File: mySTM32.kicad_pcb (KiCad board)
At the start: 2 copper layers, 138 x 108 mm, 122 parts, among them J1 conn1X2, J10 DB9_Female****, J11 USB_OTG, J12 conn2X16, J13 conn2X3, J14 Conn_02x02, J15 conn2X3, J16 conn1X2, J17 conn2X2, J18 JTAG, J19 Conn_02x17_Odd_Even, J2 USB_OTG, J20 Conn_02x22_Odd_Even, J21 conn2X9, J22 conn2X3, J23 Conn2x4, J3 conn2X3, J4 conn2X2, J5 conn2X2, J6 conn1X2, J7 Conn_01x02, J8 Conn2x4, J9 conn2X4, Q1 Q_NPN_BEC(S8050), Q2 Q_NPN_BEC, Q3 Q_NPN_BEC(S8050), SW1 KFT8.0, SW2 WAKUP, SW3 RESET, SW4 KE1, SW5 KEY2, U1 AT24C02, U2 W25Q16, U3 SD-Card, U4 SP3485, U5 SN65HVD230, U6 CH340G, U7 AMS1117, U8 SP3232, U9 STM32F103VET6, Y1 12MHz, Y2 32.768KHz, Y3 8MHz

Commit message: [sd-card]
Signed-off-by: EasonLiang <liangyx25@163.com>
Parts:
- moved R11 1.55 mm to (86.7, 61.9)
- moved R13 1.52 mm to (101.4, 61.8)
- moved R10 1.47 mm to (84.2, 61.9)
- moved R14 1.46 mm to (81.7, 61.9)
- moved R12 1.19 mm to (99.2, 61.9)
- moved C8 0.86 mm to (92.5, 61.1), turned to 0 degrees
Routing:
- net /PC8: track 26.4 -> 89.6 mm, vias 0 -> 1
- net /PC10: track 25.5 -> 84.2 mm, vias 0 -> 2
- net /PC9: track 23.3 -> 79.8 mm, vias 0 -> 1
- net /PC11: track 22.6 -> 76.4 mm, vias 0 -> 2
- net /PC12: track 26.4 -> 78.5 mm, vias 0 -> 1
- net /PD2: track 25.6 -> 75.7 mm, vias 0 -> 2
- net +3V3: track 262.6 -> 287.4 mm
- net /KEY1: track 34.5 -> 39.8 mm
- net /JTDI: track 76.9 -> 81.5 mm
- net /JTCK_SWCLK: track 77.0 -> 79.6 mm
- net /JTMS_SWDIO: track 74.9 -> 77.2 mm
- net /OV_PE6: track 51.8 -> 50.0 mm
- net /JTDO: track 84.3 -> 84.9 mm

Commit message: [Camera]
Signed-off-by: EasonLiang <liangyx25@163.com>
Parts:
- moved J23 6.20 mm to (54.1, 36.4)
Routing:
- net /OV_PC7: track 23.4 -> 115.3 mm, vias 0 -> 2
- net /OV_PC6: track 26.5 -> 112.7 mm, vias 0 -> 2
- net /NRF_CSN: track 50.1 -> 123.9 mm
- net /NRF_CE: track 0.00 -> 69.9 mm
- net /NRF_IRQ: track 0.00 -> 66.7 mm
- net /OV_PC5: track 30.2 -> 96.2 mm, vias 0 -> 1
- net /OV_PC4: track 32.5 -> 95.9 mm
- net /OV_PC3: track 30.2 -> 89.9 mm, vias 0 -> 1
- net /OV_PC1: track 30.5 -> 82.8 mm, vias 0 -> 2
- net /OV_PE6: track 50.0 -> 101.1 mm
- net /OV_PE4: track 50.0 -> 100.1 mm
- net /OV_PE3: track 47.0 -> 96.9 mm
- net /OV_PE5: track 46.9 -> 96.9 mm
- net /OV_PC2: track 33.3 -> 81.7 mm, vias 0 -> 1
- net /OV_PC0: track 34.1 -> 82.2 mm, vias 0 -> 2
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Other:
- board text added: "PC0"
- board text added: "PC1"
- board text added: "PC2"
- board text added: "PC3"
- board text added: "PC4"
- board text added: "PC5"
- board text added: "PC6"
- board text added: "PC7"
- board text added: "PE0"
- board text added: "PE1"
- board text added: "PE2"
- board text added: "PE3"
- board text added: "PE4"
- board text added: "PE5"
- board text added: "PE6"
- board text added: "X"

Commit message: [RF2.4G]
Signed-off-by: EasonLiang <liangyx25@163.com>
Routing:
- net /PA6: track 52.0 -> 137.4 mm, vias 0 -> 1
- net /PA7: track 51.6 -> 136.7 mm, vias 0 -> 1
- net /PA5: track 52.3 -> 132.8 mm, vias 0 -> 1
- net +3V3: track 287.3 -> 363.9 mm
- net GND: track 121.3 -> 123.0 mm, vias 2 -> 3
- net /FLASH_CS: track 16.6 -> 18.1 mm
- net /FLASH_MOSI: track 10.3 -> 11.7 mm
- net /OV_PC3: track 89.9 -> 91.0 mm, vias 1 -> 2
- net /FLASH_CLK: track 9.83 -> 10.4 mm, vias 0 -> 1
- net /KEY1: vias 1 -> 2

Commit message: [TFT-LCD]
Signed-off-by: EasonLiang <liangyx25@163.com>
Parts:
- moved SW2 15.0 mm to (82.9, 132.7)
- moved SW3 14.9 mm to (68.0, 132.7)
- moved R21 4.91 mm to (117.3, 121.2), turned to 0 degrees
- moved C22 1.15 mm to (102.5, 109.7), turned to 180 degrees
- moved R19 0.20 mm to (75.3, 125.6)
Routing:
- net /FSMC_NE1: track 32.3 -> 84.7 mm, vias 0 -> 2
- net /FSMC_NOE: track 27.0 -> 73.8 mm, vias 0 -> 2
- net /DB2: track 24.1 -> 70.6 mm, vias 0 -> 2
- net /FSMC_NWE: track 30.8 -> 75.5 mm, vias 0 -> 2
- net /DB3: track 27.9 -> 72.3 mm, vias 0 -> 2
- net /FSMC_A16: track 26.5 -> 70.3 mm, vias 0 -> 2
- net /BL_CTR: track 26.2 -> 67.7 mm, vias 0 -> 1
- net /DB4: track 33.1 -> 70.4 mm, vias 0 -> 1
- net /DB6: track 34.6 -> 71.1 mm, vias 0 -> 1
- net /DB5: track 36.9 -> 72.5 mm, vias 0 -> 1
- net /RESET: track 14.7 -> 49.1 mm, vias 0 -> 1
- net /DB8: track 38.1 -> 72.5 mm, vias 0 -> 1
- net +3V3: track 363.9 -> 397.0 mm
- net /DB0: track 27.3 -> 59.4 mm, vias 0 -> 2
- net /DB10: track 37.5 -> 68.6 mm, vias 0 -> 1
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
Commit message: [Key Array]
Signed-off-by: EasonLiang <liangyx25@163.com>
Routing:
- net /RESET: track 49.1 -> 167.5 mm
- net /KEY1: track 52.9 -> 126.0 mm, vias 2 -> 3
- net /KEY2: track 38.2 -> 102.5 mm, vias 0 -> 2
- net /PA0: track 39.7 -> 89.4 mm, vias 0 -> 2
- net /DB8: track 72.5 -> 55.0 mm
- net /JTMS_SWDIO: track 72.8 -> 65.4 mm
- net /JTDI: track 75.5 -> 81.5 mm
- net /PC10: track 84.2 -> 88.5 mm
- net /DB3: track 72.3 -> 76.0 mm
- net /JTDO: track 90.2 -> 87.1 mm
- net /DB2: track 70.6 -> 67.8 mm
- net /PD2: track 75.5 -> 77.7 mm
- net /PC11: track 77.2 -> 79.1 mm
- net GND: track 123.0 -> 124.3 mm, vias 3 -> 4
- net /PD13: track 50.2 -> 51.3 mm
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
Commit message: [boot] partial
Signed-off-by: EasonLiang <liangyx25@163.com>
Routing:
- net /BOOT0: track 0.00 -> 71.8 mm, vias 0 -> 2
- net +3V3: track 397.0 -> 430.8 mm, vias 6 -> 9

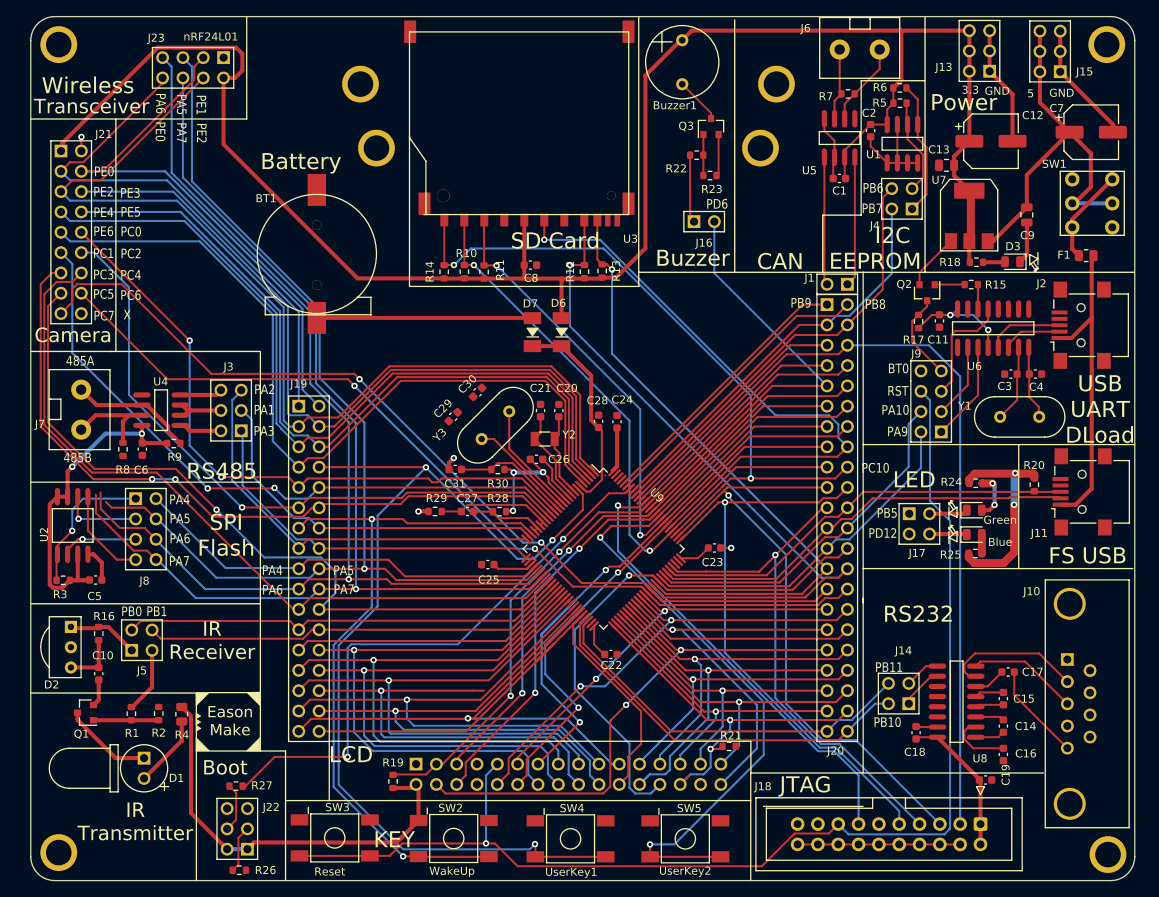
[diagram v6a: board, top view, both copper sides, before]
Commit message: [Power] [Boot] [Reset] [nRF IRQ/CE]
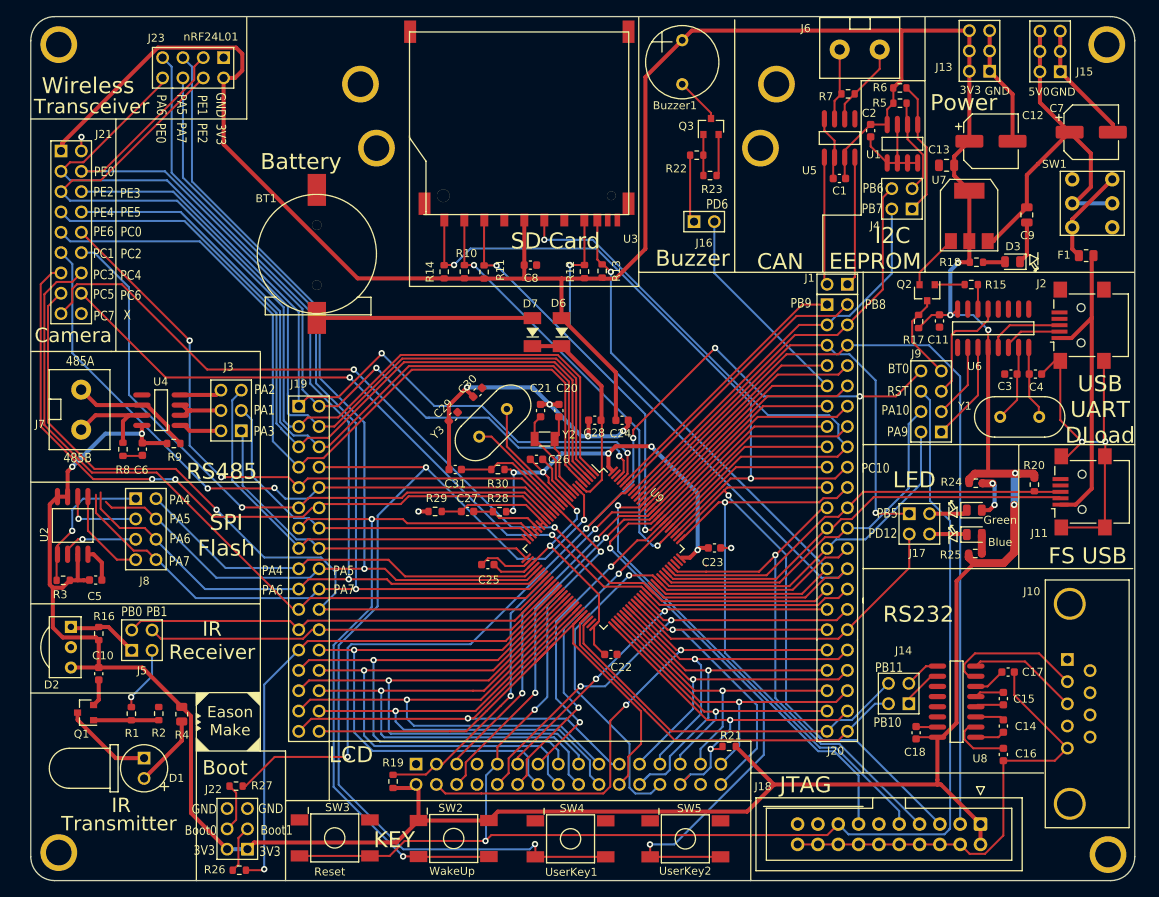
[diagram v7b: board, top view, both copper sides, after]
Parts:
- removed C19: 0.1uF, Capacitor_SMD:C_0603_1608Metric
- moved C24 0.66 mm to (103.9, 80.5), turned to 180 degrees
- moved C28 0.49 mm to (100.5, 80.5), turned to 0 degrees
- moved Y3 0.42 mm to (86.1, 82.5)
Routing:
- net +3V3: track 430.8 -> 642.3 mm, vias 9 -> 15
- net GND: track 124.3 -> 245.4 mm, vias 4 -> 9
- net /BOOT0: track 71.8 -> 130.8 mm, vias 2 -> 5
- net /NRF_IRQ: track 66.7 -> 119.4 mm, vias 0 -> 2
- net /NRF_CE: track 69.9 -> 117.5 mm, vias 0 -> 2
- net /RESET: track 167.5 -> 204.4 mm, vias 1 -> 3
- net /BOOT1: track 35.5 -> 67.0 mm, vias 0 -> 1
- net /LED1: track 31.4 -> 60.1 mm, vias 0 -> 1
- net /DB8: track 55.0 -> 70.4 mm
- net /LED2: track 28.8 -> 43.9 mm
- net /DB3: track 76.0 -> 68.2 mm
- net /OV_PE3: track 96.9 -> 99.4 mm
- net /OV_PE4: track 100.1 -> 102.6 mm
- net /OV_PE5: track 96.9 -> 99.3 mm
- net /OV_PE6: track 101.1 -> 103.6 mm
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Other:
- board text added: "3V3"
- board text added: "5V0"
- board text added: "Boot0"
- board text added: "Boot1"
- board text added: "IR"
- board text added: "Transmitter"
- board text removed: "3.3"
- board text removed: "5"
- board text removed: "IR Transmitter"

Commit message: [Annotation]
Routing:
- net +3V3: track 642.3 -> 646.0 mm
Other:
- board text added: "A1"
- board text added: "A10"
- board text added: "A12"
- board text added: "A2"
- board text added: "A3"
- board text added: "B12"
- board text added: "B14"
- board text added: "B5"
- board text added: "D12"
- board text added: "PA0"
- board text added: "PA11"
- board text added: "PA13"
- board text added: "PA14"
- board text added: "PA15"
- board text added: "PA8"
- board text added: "PB13"
- board text added: "PB15"
- board text added: "PB2"
- board text added: "PB3"
- board text added: "PB4"
- board text added: "PC11"
- board text added: "PC12"
- board text added: "PC13"
- board text added: "PC8"
- board text added: "PC9"
- board text added: "PD0"
- board text added: "PD1"
- board text added: "PD10"
- board text added: "PD11"
- board text added: "PD13"
- board text added: "PD14"
- board text added: "PD15"
- board text added: "PD2"
- board text added: "PD3"
- board text added: "PD4"
- board text added: "PD5"
- board text added: "PD7"
- board text added: "PD8"
- board text added: "PD9"
- board text added: "PE10"
- board text added: "PE11"
- board text added: "PE12"
- board text added: "PE13"
- board text added: "PE14"
- board text added: "PE15"
- board text added: "PE7"
- board text added: "PE8"
- board text added: "PE9"
- board text added: "SWCLK"
- board text added: "SWDIO"
- board text added: "nRST"
